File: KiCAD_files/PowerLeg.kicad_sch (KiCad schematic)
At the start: 83 parts, among them Q201 IPD200N15N3, Q202 IPD200N15N3, Q203 DMN10H220L-7, Q204 DMP3099-x, U201 AMC1100DUB, U202 ACS730xLCTR-20AB, U203 UCC21222DR, U204 MCP6486UT-E/LT, U205 MCP6486UT-E/LT, U206 FODM217A, U207 FODM217A

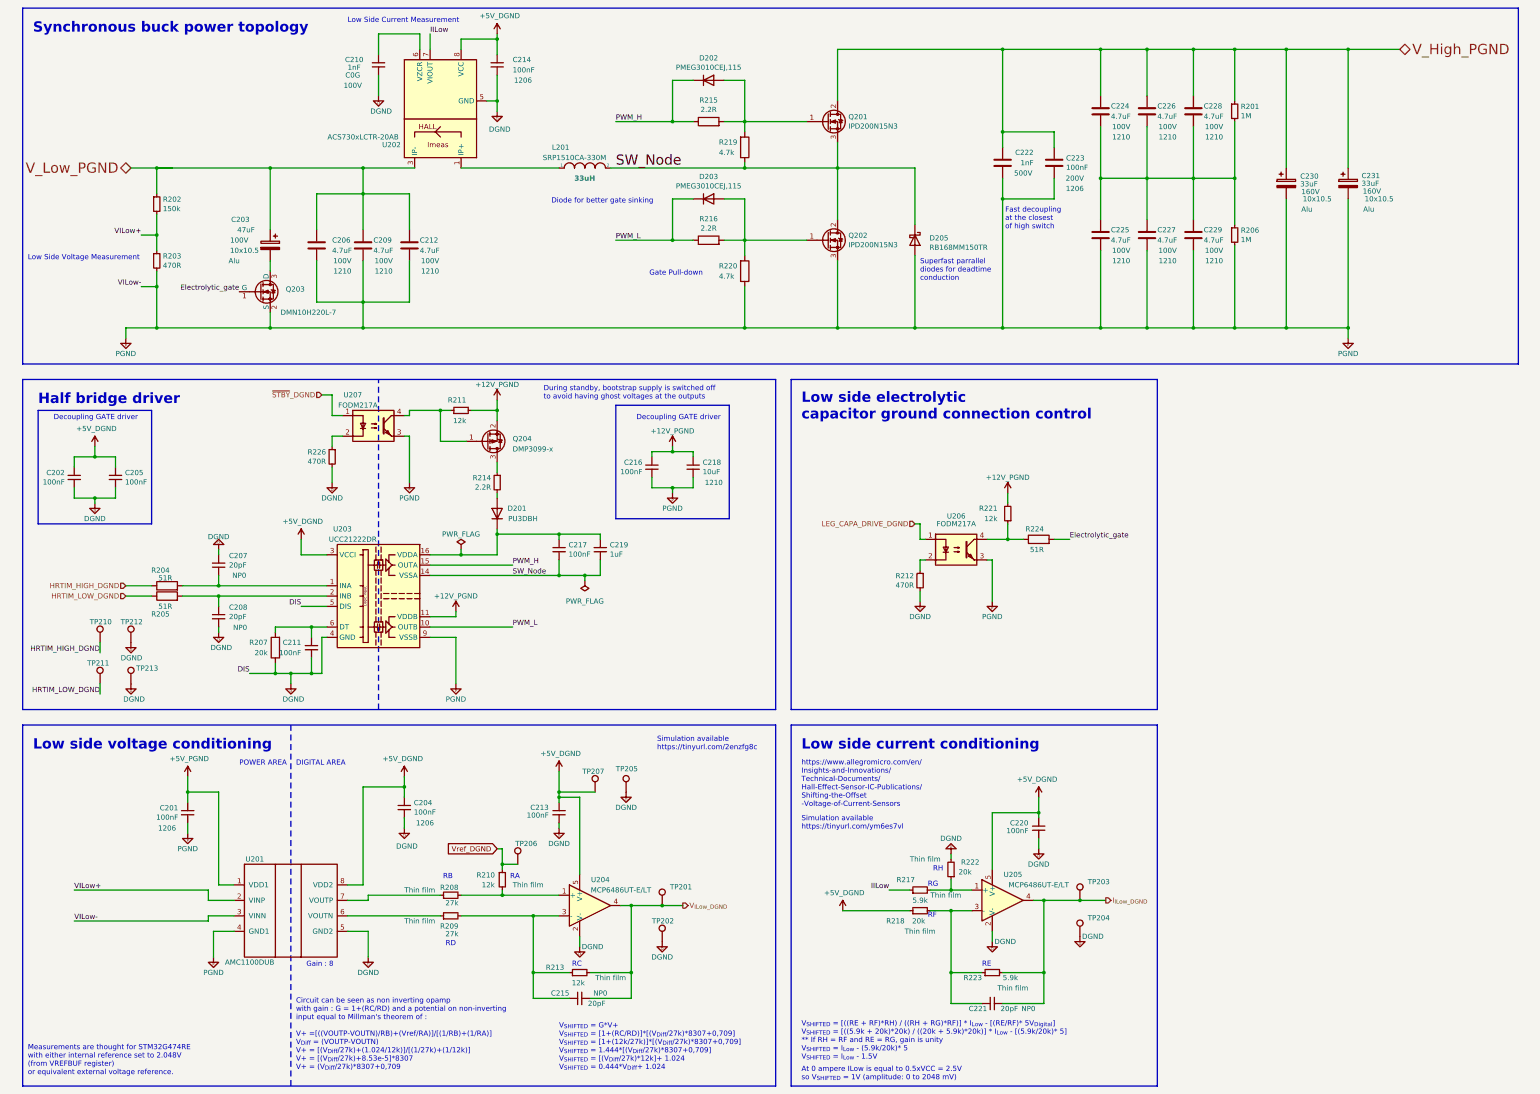
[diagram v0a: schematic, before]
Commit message: Rule zones added, DRC rules added, Added FPC connectors
Signed-off-by: Jean Alinei <jean.alinei@owntech.org>
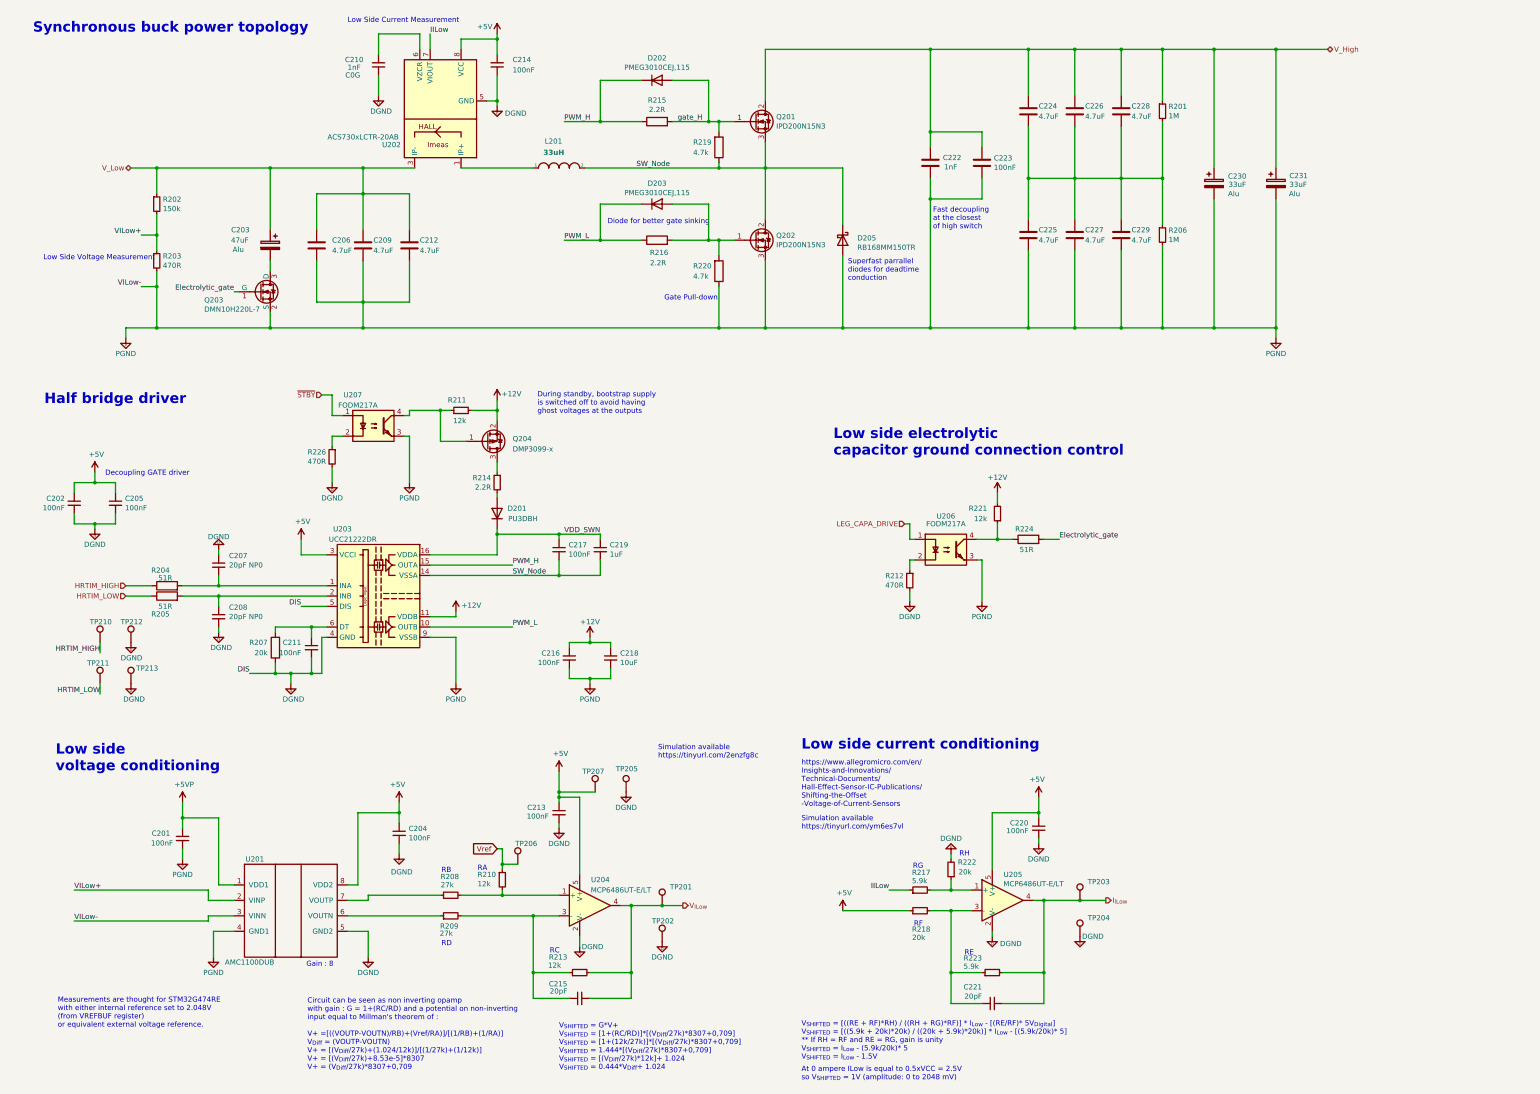
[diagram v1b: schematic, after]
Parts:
- C201, C202, C204, C205, C211, C213, C214, C216, C217, C220: Package 1206 -> (none); Voltage 50V -> (none); Voltage_Rating (none) -> 50V
- C203: Package 10x10.5 -> (none); VRating 100V -> (none); Voltage 100V -> (none); Voltage_Rating (none) -> 100V
- C206, C209, C212, C224, C225, C226, C227, C228, C229: Package 1210 -> (none); VRating 100V -> (none); Voltage 100V -> (none); Voltage_Rating (none) -> 100V
- C207, C208, C215, C219, C221: Package 0805 -> (none); Voltage 50V -> (none); Voltage_Rating (none) -> 50V
- C210: Package 0805 -> (none); Voltage 100V -> (none); Voltage_Rating (none) -> 100V
- C218: Package 1210 -> (none); Voltage 50V -> (none); Voltage_Rating (none) -> 50V
- C222: Package 0805 -> (none); VRating 500V -> (none); Voltage 500V -> (none); Voltage_Rating (none) -> 500V
- C223: Package 1206 -> (none); VRating 200V -> (none); Voltage 200V -> (none); Voltage_Rating (none) -> 200V
- C230, C231: Package 10x10.5 -> (none); VRating 160V -> (none); Voltage 160V -> (none); Voltage_Rating (none) -> 160V
- R201, R202, R203, R204, R205, R206, R212, R214, R215, R216, R219, R220, R224, R226: Package 0805 -> (none); Technology Thick film -> (none)
- R207, R208, R209, R210, R211, R213, R217, R218, R221, R222, R223: Package 0805 -> (none); Technology Thin film -> (none)
- TP201, TP202, TP203, TP204, TP205, TP206, TP207, TP210, TP211, TP212, TP213: DNP x -> (none)
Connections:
- net VDD_SWN: now reaches C217.1, C219.1, D201.1 (K), U203.16 (VDDA)
- net gate_H: now reaches D202.2 (A), Q201.1 (G), R215.2, R219.2
- net +12V_PGND renamed +12V
- net +5V_DGND renamed +5V
- net +5V_PGND renamed +5VP
- net HRTIM_HIGH_DGND renamed HRTIM_HIGH
- net HRTIM_LOW_DGND renamed HRTIM_LOW
- net I_{ILow_DGND} renamed I_{ILow}
- net LEG_CAPA_DRIVE_DGND renamed LEG_CAPA_DRIVE
- net V_High_PGND renamed V_High
- net V_Low_PGND renamed V_Low
- net V_{ILow_DGND} renamed V_{ILow}
- net Vref_DGND renamed Vref
- net ~{STBY}_DGND renamed ~{STBY}
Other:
- note removed: "DIGITAL AREA"
- note removed: "POWER AREA"
- company: https://gitlab.laas.fr/owntech/boards/TWIST -> https://github.com/owntech-foundation/twist
- title: TWIST 1.4 -> TWIST 1.4.2
- moved on the sheet: C201, C202, C204, C205, C216, C218, C222, C223, C224, C225, C226, C227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
